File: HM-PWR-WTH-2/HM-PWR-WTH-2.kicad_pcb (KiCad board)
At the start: 2 copper layers, 45 x 43 mm, 42 parts, among them J101 Screw_Terminal_01x02, J102 Conn_01x02_Male, J103 Conn_01x02_Male, J104 Conn_01x02_Male, J105 Conn_01x02_Male, J106 USB_B_Micro, SW101 SW_Push, SW102 SW_Push, U101 LT8606xMSE

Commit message: HM-PWR-WTH-2: Switch to TPS70930
Signed-off-by: Patrick Rudolph <patrick.rudolph@9elements.com>
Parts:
- removed C101: 1u, Capacitor_SMD:C_0805_2012Metric_Pad1.18x1.45mm_HandSolder
- removed C105: 100n, Capacitor_SMD:C_0603_1608Metric_Pad1.08x0.95mm_HandSolder
- removed C106: 10n, Capacitor_SMD:C_0603_1608Metric_Pad1.08x0.95mm_HandSolder
- removed C107: 10p, Capacitor_SMD:C_0603_1608Metric_Pad1.08x0.95mm_HandSolder
- removed C116, C117: 4u7, Capacitor_SMD:C_1206_3216Metric_Pad1.33x1.80mm_HandSolder
- removed L102: 242408FPS-6R8M-01, Inductor_SMD:L_Bourns-SRN6028
- removed R102: 100k, Resistor_SMD:R_0603_1608Metric_Pad0.98x0.95mm_HandSolder
- removed R103: 1meg, Resistor_SMD:R_0805_2012Metric_Pad1.20x1.40mm_HandSolder
- removed R105: 18k2, Resistor_SMD:R_0603_1608Metric_Pad0.98x0.95mm_HandSolder
- removed R106: 330k, Resistor_SMD:R_0603_1608Metric_Pad0.98x0.95mm_HandSolder
- removed R107: 22k, Resistor_SMD:R_0603_1608Metric_Pad0.98x0.95mm_HandSolder
- U101: value LT8606xMSE -> TPS70930QDBVRQ1; footprint Package_SO:MSOP-10-1EP_3x3mm_P0.5mm_EP1.68x1.88mm -> Package_TO_SOT_SMD:SOT-23-5_HandSoldering
- moved L101 10.6 mm to (102.0, 108.0)
- moved C103 9.94 mm to (97.0, 106.2), turned to 90 degrees
- moved U101 9.03 mm to (103.5, 96.0), turned to 90 degrees
- moved C104 8.26 mm to (103.3, 103.5), turned to 180 degrees
- moved C109 6.91 mm to (103.6, 100.0), turned to 0 degrees
- moved FB101 5.39 mm to (92.8, 107.8), turned to 180 degrees
- moved R108 2.61 mm to (78.8, 100.5), turned to 270 degrees
- moved D103 2.09 mm to (81.8, 98.1)
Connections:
- J101 pad 2: GND -> Net-(J101-Pad2)
- U101 pad 1: Net-(C105-Pad2) -> +24V
- U101 pad 2: Net-(C105-Pad1) -> GND
- U101 pad 3: Net-(C101-Pad2) -> Net-(U101-Pad3)
- U101 pad 5: Net-(C101-Pad2) -> 3V0
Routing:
- net 3V0: track 118.1 -> 88.1 mm, vias 4 -> 3
- net Net-(R102-Pad2): track 15.2 -> 0.00 mm, vias 2 -> 0
- net Net-(C101-Pad2): track 8.56 -> 0.00 mm, vias 2 -> 0
- net Net-(C107-Pad2): track 8.47 -> 0.00 mm
- net Net-(C105-Pad1): track 6.24 -> 0.00 mm
- net VIN: track 6.60 -> 12.4 mm
- net Net-(C106-Pad2): track 4.46 -> 0.00 mm
- net Net-(U101-Pad4): track 3.64 -> 0.00 mm
- net +24V: track 8.86 -> 11.8 mm
- net GND: track 1.28 -> 4.23 mm, vias 44 -> 27
- net Net-(C105-Pad2): track 2.52 -> 0.00 mm
- net Net-(R106-Pad2): track 2.40 -> 0.00 mm
- net Net-(D103-Pad1): track 9.75 -> 11.8 mm
- net Net-(C103-Pad1): track 7.57 -> 6.84 mm
- removed copper zone on B.Cu, net 3V0
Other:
- board text added: "HM-PWR-WTH-2"
- board text added: "Test"

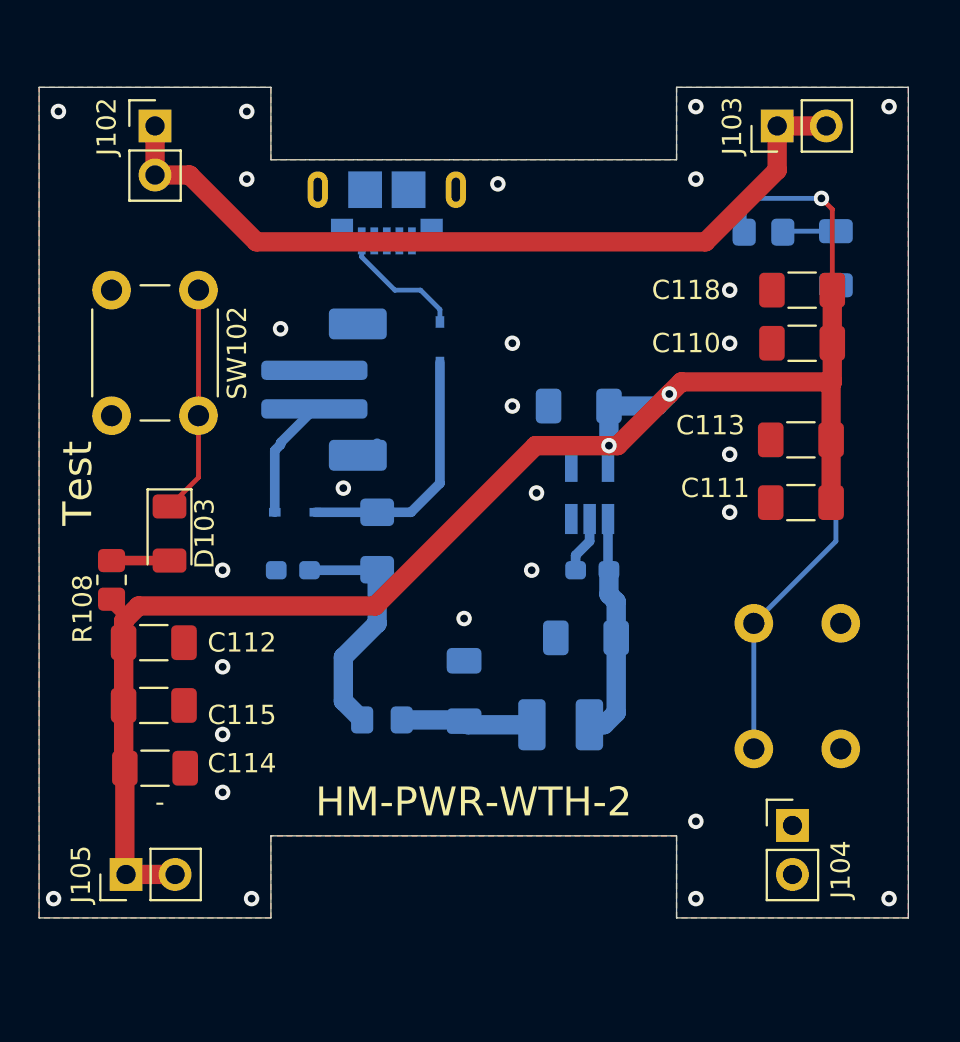
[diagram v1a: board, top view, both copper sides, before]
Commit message: Redesign board
- Replace regulator with one easier to get in germany
- Add LED for minimum current draw of 1mA
- Swap battery + and -

Signed-off-by: Patrick Rudolph <patrick.rudolph@9elements.com>
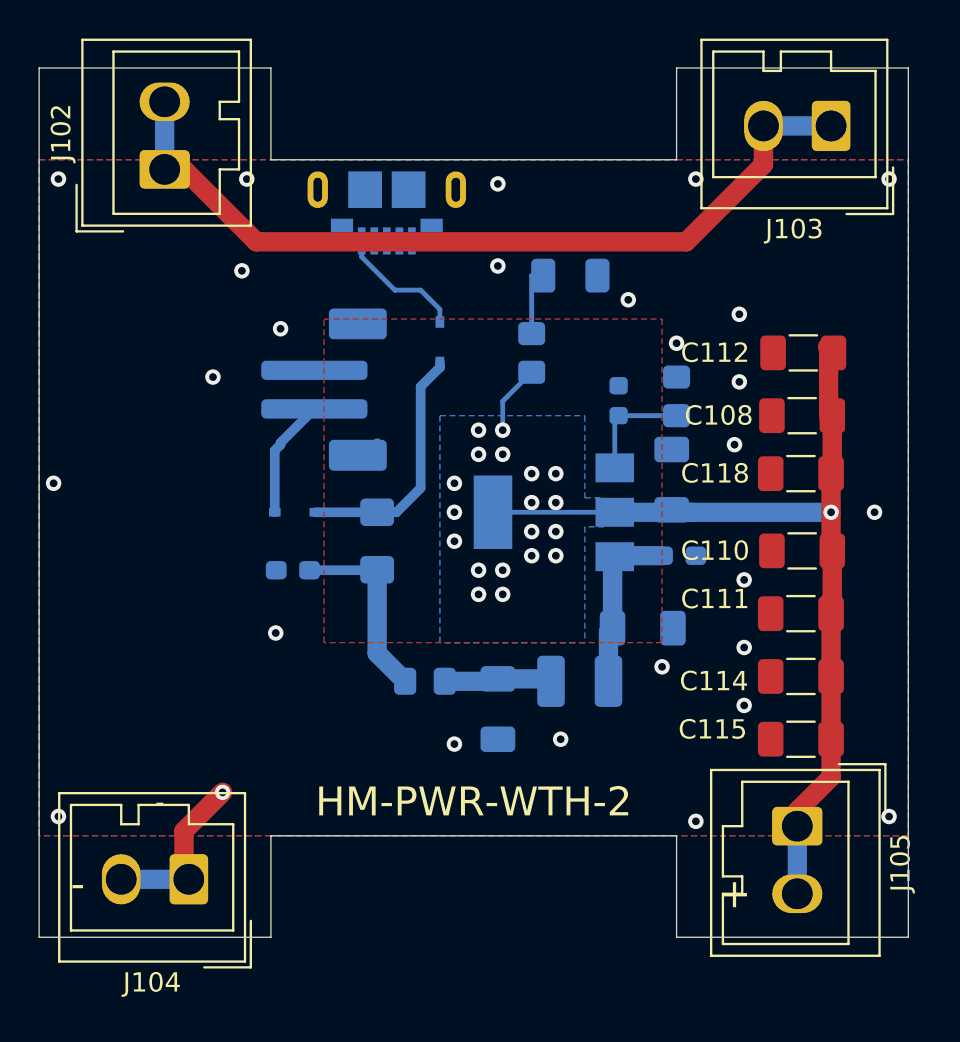
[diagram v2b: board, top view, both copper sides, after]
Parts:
- removed D103: LED, LED_SMD:LED_1206_3216Metric
- removed R108: 1k, Resistor_SMD:R_0805_2012Metric_Pad1.20x1.40mm_HandSolder
- removed SW101, SW102: SW_Push, Button_Switch_THT:SW_PUSH_6mm_H5mm
- added C101: 10p, Capacitor_SMD:C_0603_1608Metric, B.Cu at (105.0, 91.2)
- added R101: 287k, Resistor_SMD:R_0805_2012Metric_Pad1.20x1.40mm_HandSolder, B.Cu at (108.0, 91.0)
- C108: moved to F.Cu
- C113: moved to B.Cu
- J102, J103, J104, J105: footprint Connector_PinHeader_2.54mm:PinHeader_1x02_P2.54mm_Vertical -> Connector_Wago:Wago_734-132_1x02_P3.50mm_Vertical
- R104: value 1k -> 1k5
- U101: value TPS70930QDBVRQ1 -> LT3080xST; footprint Package_TO_SOT_SMD:SOT-23-5_HandSoldering -> Package_TO_SOT_SMD:SOT-223
- moved C112 36.8 mm to (114.6, 88.8), turned to 180 degrees
- moved J105 34.8 mm to (114.2, 113.2), turned to 270 degrees
- moved C114 33.8 mm to (114.4, 105.5), turned to 180 degrees
- moved C115 33.5 mm to (114.4, 108.8), turned to 180 degrees
- moved J104 31.4 mm to (82.8, 116.0), turned to 180 degrees
- moved D102 13.8 mm to (102.5, 84.8), turned to 180 degrees
- moved R104 13.5 mm to (100.5, 88.8), turned to 270 degrees
- moved C108 11.6 mm to (114.5, 92.0)
- moved C110 10.8 mm to (114.5, 99.0)
- moved C118 9.50 mm to (114.4, 95.0)
- moved C113 7.00 mm to (107.8, 95.3), turned to 90 degrees
- moved C111 5.75 mm to (114.4, 102.2)
- moved C109 4.56 mm to (108.1, 99.2), turned to 180 degrees
- moved FB101 2.99 mm to (95.0, 105.8)
- moved C104 2.98 mm to (106.2, 103.0), turned to 0 degrees
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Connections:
- D102 pad 1: Net-(D102-Pad1) -> GND
- J101 pad 2: Net-(J101-Pad2) -> GND
- U101 pad 1: +24V -> Net-(C101-Pad2)
- U101 pad 2: GND -> 3V0
- U101 pad 3: Net-(U101-Pad3) -> +24V
- U101 pad 4: Net-(U101-Pad4) -> 3V0
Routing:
- net 3V0: track 88.1 -> 50.3 mm, vias 3 -> 20
- net Net-(D102-Pad1): track 25.8 -> 0.00 mm
- net Net-(D103-Pad1): track 11.8 -> 0.00 mm
- net GND: track 4.23 -> 10.3 mm, vias 27 -> 26
- net Net-(C101-Pad2): track 0.00 -> 5.78 mm
- net Net-(D103-Pad2): track 3.00 -> 0.00 mm
- net +24V: track 11.8 -> 9.08 mm
- net VIN: track 12.4 -> 9.89 mm
- net Net-(C103-Pad1): track 6.84 -> 5.60 mm
- net Net-(D102-Pad2): track 2.77 -> 3.60 mm
- net Net-(J102-Pad1): track 42.5 -> 43.2 mm
- net (no net): vias 0 -> 1
- added copper zone on B.Cu, net 3V0
- added copper zone on F.Cu, net 3V0
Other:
- board size 45 x 43 mm -> 45 x 45 mm
- board text added: "+"
- board text removed: "Test"

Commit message: Redesign board
- Move all parts to middle and back
- Use less capacitors
- Add mounting holes
- Add battery symbols

Signed-off-by: Patrick Rudolph <patrick.rudolph@9elements.com>
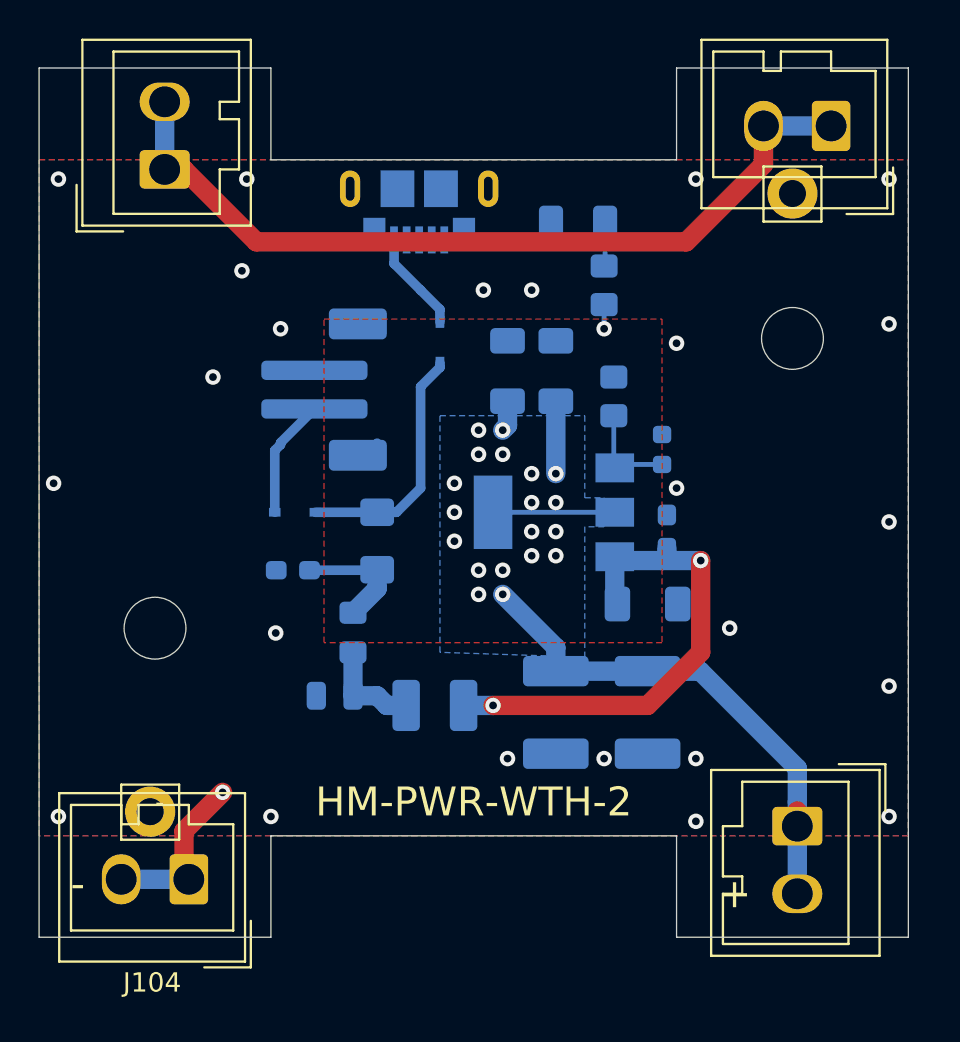
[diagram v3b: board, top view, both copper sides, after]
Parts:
- removed C110, C112, C113, C115: 4u7, Capacitor_SMD:C_1206_3216Metric_Pad1.33x1.80mm_HandSolder
- added H101: MountingHole, MountingHole:MountingHole_3.2mm_M3_ISO14580, F.Cu at (114.0, 88.0)
- added H102: MountingHole, MountingHole:MountingHole_3.2mm_M3, F.Cu at (81.2, 103.8)
- added J107: Conn_01x01_Male, Connector_Pin:Pin_D1.4mm_L8.5mm_W2.8mm_FlatFork, F.Cu at (80.8, 112.5)
- added J108: Conn_01x01_Male, Connector_Pin:Pin_D1.4mm_L8.5mm_W2.8mm_FlatFork, F.Cu at (114.0, 80.5)
- C103: value 33u -> 100n; footprint Capacitor_SMD:C_1206_3216Metric_Pad1.33x1.80mm_HandSolder -> Capacitor_SMD:C_0805_2012Metric
- C108, C118: moved to B.Cu
- C111, C114: value 4u7 -> 33u; footprint Capacitor_SMD:C_1206_3216Metric_Pad1.33x1.80mm_HandSolder -> Capacitor_SMD:C_1812_4532Metric_Pad1.57x3.40mm_HandSolder; moved to B.Cu
- moved C108 15.4 mm to (99.2, 89.7), turned to 270 degrees
- moved C118 13.8 mm to (101.8, 89.7), turned to 270 degrees
- moved C111 13.7 mm to (101.8, 107.4), turned to 270 degrees
- moved C103 8.48 mm to (90.3, 106.5), turned to 180 degrees
- moved C114 8.15 mm to (106.5, 107.4), turned to 270 degrees
- moved L101 7.60 mm to (95.5, 107.0)
- moved R104 5.13 mm to (104.2, 85.2)
- moved FB101 4.50 mm to (91.2, 103.2), turned to 90 degrees
- moved C101 3.38 mm to (107.2, 93.8)
- moved R101 3.25 mm to (104.8, 91.0)
- moved D102 2.78 mm to (102.9, 82.0), turned to 0 degrees
- moved J106 1.68 mm to (94.7, 81.5)
- moved C109 1.40 mm to (107.5, 98.0), turned to 270 degrees
- moved C104 1.27 mm to (106.5, 101.8)
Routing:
- net +24V: track 9.08 -> 26.2 mm, vias 0 -> 2
- net 3V0: track 50.3 -> 39.9 mm
- net VIN: track 9.89 -> 6.25 mm
- net Net-(D104-Pad2): track 6.66 -> 5.23 mm
- net Net-(D102-Pad2): track 3.60 -> 2.27 mm
- net Net-(C101-Pad2): track 5.78 -> 5.24 mm
- net GND: vias 26 -> 24
